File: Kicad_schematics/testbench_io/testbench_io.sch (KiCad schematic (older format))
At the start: 43 parts, among them J101 Conn_01x02, J102 Conn_01x02, J103 Conn_01x02, J104 DB37_Female_MountingHoles, SW101 SW_SPST, SW102 SW_Push, SW103 SW_Push, SW104 SW_Push, SW105 SW_Push, SW106 SW_SPST, SW107 SW_SPST, SW108 SW_DIP_x08, SW109 SW_SPST, SW110 SW_Push, SW111 SW_SPST, SW112 SW_SPST, SW113 SW_SPST, SW114 SW_DPDT_x2, U101 NUCLEO64-F476RG, U102 CJMCU_MCP2551

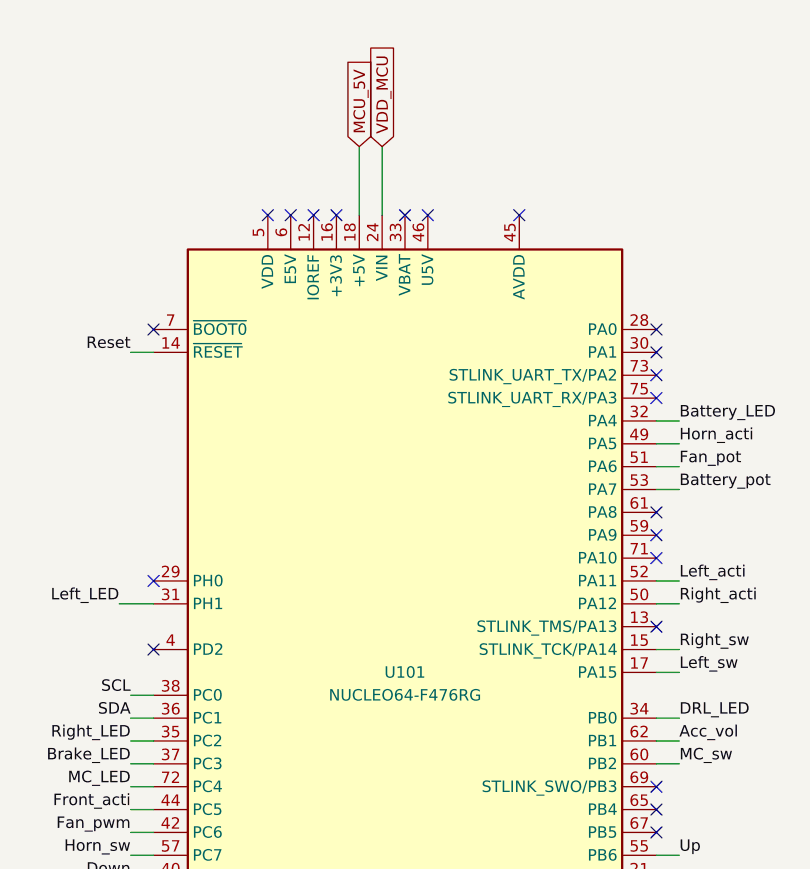
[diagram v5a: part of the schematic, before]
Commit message: Fixed some footprints
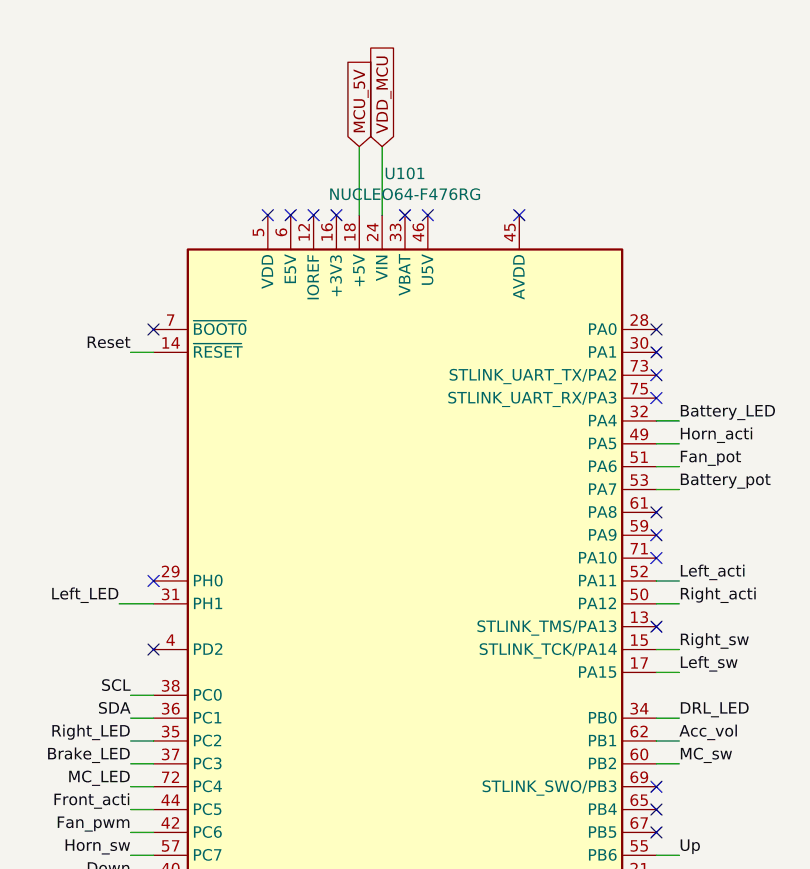
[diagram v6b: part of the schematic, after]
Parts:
- removed U101: NUCLEO64-F476RG, Solar_team:MODULE_NUCLEO-F476RG, symbol MCU_Module:NUCLEO64-F411RE
- added U101: NUCLEO64-F476RG, Solar_team:MODULE_NUCLEO-F476RG, symbol Solarteam:NUCLEO64-F476RG
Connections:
- net Acc_vol: now also U101.62 (PB1)
- net Battery_LED: now also U101.32 (PA4)
- net Battery_pot: now also U101.53 (PA7)
- net Brake_LED: now also U101.37 (PC3)
- net Brake_acti: now also U101.54 (PB12)
- net Brake_vol: now also U101.64 (PB15)
- net CRX: now also U101.41 (PB8)
- net CTX: now also U101.43 (PB9)
- net DRL_LED: now also U101.34 (PB0)
- net DRL_sw: now also U101.25 (PC14)
- net Down: now also U101.40 (PC8)
- net F-R_sw: now also U101.68 (PB13)
- net Fan_pot: now also U101.51 (PA6)
- net Fan_pwm: now also U101.42 (PC6)
- net Front_acti: now also U101.44 (PC5)
- net GND: now also U101.8 (GND)
- net HL_sw: now also U101.23 (PC13)
- net Horn_acti: now also U101.49 (PA5)
- net Horn_sw: now also U101.57 (PC7)
- net Left_LED: now also U101.31 (PH1)
- net Left_acti: now also U101.52 (PA11)
- net Left_sw: now also U101.17 (PA15)
- net MCU_5V: now also U101.18 (+5V)
- net MC_LED: now also U101.72 (PC4)
- net MC_sw: now also U101.60 (PB2)
- net P-E_sw: now also U101.66 (PB14)
- net Reset: now also U101.14 (~RESET)
- net Right_LED: now also U101.35 (PC2)
- net Right_acti: now also U101.50 (PA12)
- net Right_sw: now also U101.15 (STLINK_TCK/PA14)
- net SCL: now also U101.38 (PC0)
- net SDA: now also U101.36 (PC1)
- net Select: now also U101.39 (PC9)
- net Up: now also U101.55 (PB6)
- net VDD_MCU: now also U101.24 (VIN)
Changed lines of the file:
@@
 $EndDescr
-$Comp
-L MCU_Module:NUCLEO64-F411RE U101
-U 1 1 5FF2E5E7
-P 2800 4900
-F 0 "U101" H 2800 4900 50  0000 C CNN
-F 1 "NUCLEO64-F476RG" H 2800 4800 50  0000 C CNN
-F 2 "Solar_team:MODULE_NUCLEO-F476RG" H 3350 3000 50  0001 L CNN
-F 3 "http://www.st.com/st-web-ui/static/active/en/resource/technical/document/data_brief/DM00105918.pdf" H 1900 3500 50  0001 C CNN
-	1    2800 4900
-	1    0    0    -1
-$EndComp
 $Comp
 L Device:R_POT RV103
@@
 Text GLabel 6900 4750 0    50   Input ~ 0
 GND
+$Comp
+L Solarteam:NUCLEO64-F476RG U101
+U 1 1 601A040E
+P 2800 4900
+F 0 "U101" H 2800 7081 50  0000 C CNN
+F 1 "NUCLEO64-F476RG" H 2800 6990 50  0000 C CNN
+F 2 "Solar_team:MODULE_NUCLEO-F476RG" H 3350 3000 50  0001 L CNN
+F 3 "http://www.st.com/st-web-ui/static/active/en/resource/technical/document/data_brief/DM00105918.pdf" H 1900 3500 50  0001 C CNN
+	1    2800 4900
+	1    0    0    -1
+$EndComp
 $EndSCHEMATC

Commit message: Fixed some final stuff
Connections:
- net Brake_LED: now also U101.65 (PB4); no longer U101.37 (PC3)
- net GND: now also U101.19 (GND), U101.20 (GND), U101.22 (GND), U101.47 (GND), U101.58 (GND), U101.77 (GND), U101.78 (GND), U101.79 (GND), U101.80 (GND)
- net Left_LED: now also U101.61 (PA8); no longer U101.31 (PH1)
- net Right_LED: now also U101.63 (PB10); no longer U101.35 (PC2)
- no-connect marks 60 -> 50
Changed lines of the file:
@@
 	3900 5700 4000 5700
 Wire Wire Line
-	1700 5200 1600 5200
+	3900 6100 4000 6100
 Wire Wire Line
 	3900 5300 4000 5300
-Wire Wire Line
-	3900 6500 4000 6500
 Wire Wire Line
 	3900 6300 4000 6300
@@
 Text Label 4000 5300 0    50   ~ 0
 MC_sw
-Text Label 1550 4600 2    50   ~ 0
+Text Label 4050 4200 0    50   ~ 0
 Left_LED
-Text Label 1600 5200 2    50   ~ 0
+Text Label 4000 6100 0    50   ~ 0
 Right_LED
-Text Label 4000 6500 0    50   ~ 0
-Brake_vol
 Text Label 4000 6300 0    50   ~ 0
 F-R_sw
@@
 Text Label 1600 5900 2    50   ~ 0
 Select
-Text Label 1600 5300 2    50   ~ 0
+Text Label 4000 5500 0    50   ~ 0
 Brake_LED
 Text Label 4000 4900 0    50   ~ 0
 Left_sw
-Text Label 4000 4800 0    50   ~ 0
-Right_sw
 Wire Wire Line
 	4000 4900 3900 4900
-Wire Wire Line
-	4000 4800 3900 4800
 Text GLabel 2700 2600 1    50   Input ~ 0
 VDD_MCU
@@
 NoConn ~ 3900 5800
 NoConn ~ 1700 6100
-NoConn ~ 3900 6100
 NoConn ~ 3900 4700
-NoConn ~ 3900 4200
-NoConn ~ 2300 6900
-NoConn ~ 2400 6900
-NoConn ~ 2500 6900
-NoConn ~ 2600 6900
-NoConn ~ 2700 6900
-NoConn ~ 2800 6900
-NoConn ~ 2900 6900
-NoConn ~ 3000 6900
-NoConn ~ 3100 6900
-NoConn ~ 3300 6900
+NoConn ~ 1700 5300
 NoConn ~ 3900 3500
 NoConn ~ 3900 3400
@@
 NoConn ~ 1700 6000
 NoConn ~ 1700 6500
-NoConn ~ 3900 5500
 NoConn ~ 3900 4400
 Wire Wire Line
@@
 	3900 5100 4000 5100
 Wire Wire Line
-	1700 5300 1600 5300
+	3900 5500 4000 5500
 Text Label 4000 4600 0    50   ~ 0
 Right_acti
@@
 	2950 1100 3200 1100
 Wire Wire Line
-	1550 4600 1700 4600
+	4050 4200 3900 4200
 Text GLabel 10850 650  2    50   Input ~ 0
 GND
@@
 	1    0    0    -1
 $EndComp
+NoConn ~ 1700 5200
+Wire Wire Line
+	4000 4800 3900 4800
+Text Label 4000 4800 0    50   ~ 0
+Right_sw
+NoConn ~ 1700 4600
+Text Label 4000 6500 0    50   ~ 0
+Brake_vol
+Wire Wire Line
+	3900 6500 4000 6500
+Wire Wire Line
+	2200 6900 2300 6900
+Connection ~ 2200 6900
+Connection ~ 2300 6900
+Wire Wire Line
+	2300 6900 2400 6900
+Connection ~ 2400 6900
+Wire Wire Line
+	2400 6900 2500 6900
+Connection ~ 2500 6900
+Wire Wire Line
+	2500 6900 2600 6900
+Connection ~ 2600 6900
+Wire Wire Line
+	2600 6900 2700 6900
+Connection ~ 2700 6900
+Wire Wire Line
+	2700 6900 2800 6900
+Connection ~ 2800 6900
+Wire Wire Line
+	2800 6900 2900 6900
+Connection ~ 2900 6900
+Wire Wire Line
+	2900 6900 3000 6900
+Connection ~ 3000 6900
+Wire Wire Line
+	3000 6900 3100 6900
 $EndSCHEMATC

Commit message: Change of connector
Changed a connector that wasn't available
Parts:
- J101, J102, J103: footprint Connector_JST:JST_XH_S2B-XH-A-1_1x02_P2.50mm_Horizontal -> Connector_JST:JST_XH_S2B-XH-A_1x02_P2.50mm_Horizontal
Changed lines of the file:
@@
 F 0 "J103" H 7450 2700 50  0000 L CNN
 F 1 "Conn_01x02" H 7250 2350 50  0000 L CNN
-F 2 "Connector_JST:JST_XH_S2B-XH-A-1_1x02_P2.50mm_Horizontal" H 7500 2550 50  0001 C CNN
+F 2 "Connector_JST:JST_XH_S2B-XH-A_1x02_P2.50mm_Horizontal" H 7500 2550 50  0001 C CNN
 F 3 "~" H 7500 2550 50  0001 C CNN
 	1    7500 2550
@@
 F 0 "J101" H 6100 2550 50  0000 L CNN
 F 1 "Conn_01x02" H 6000 2200 50  0000 L CNN
-F 2 "Connector_JST:JST_XH_S2B-XH-A-1_1x02_P2.50mm_Horizontal" H 6200 2400 50  0001 C CNN
+F 2 "Connector_JST:JST_XH_S2B-XH-A_1x02_P2.50mm_Horizontal" H 6200 2400 50  0001 C CNN
 F 3 "~" H 6200 2400 50  0001 C CNN
 	1    6200 2400
@@
 F 0 "J102" H 3480 992 50  0000 L CNN
 F 1 "Conn_01x02" H 3480 901 50  0000 L CNN
-F 2 "Connector_JST:JST_XH_S2B-XH-A-1_1x02_P2.50mm_Horizontal" H 3400 1000 50  0001 C CNN
+F 2 "Connector_JST:JST_XH_S2B-XH-A_1x02_P2.50mm_Horizontal" H 3400 1000 50  0001 C CNN
 F 3 "~" H 3400 1000 50  0001 C CNN
 	1    3400 1000
